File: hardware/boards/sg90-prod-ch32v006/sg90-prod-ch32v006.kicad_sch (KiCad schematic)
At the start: 36 parts, among them J1 Servo Input, J2 Motor, J3 Debug, J4 Potentiometer, Q1 AO3401A, U1 TPAP2210K-3.3TRG1, U2 74LVC2G125, U3 DRV8837DSGR-JSM, U4 CH32V006F8U6

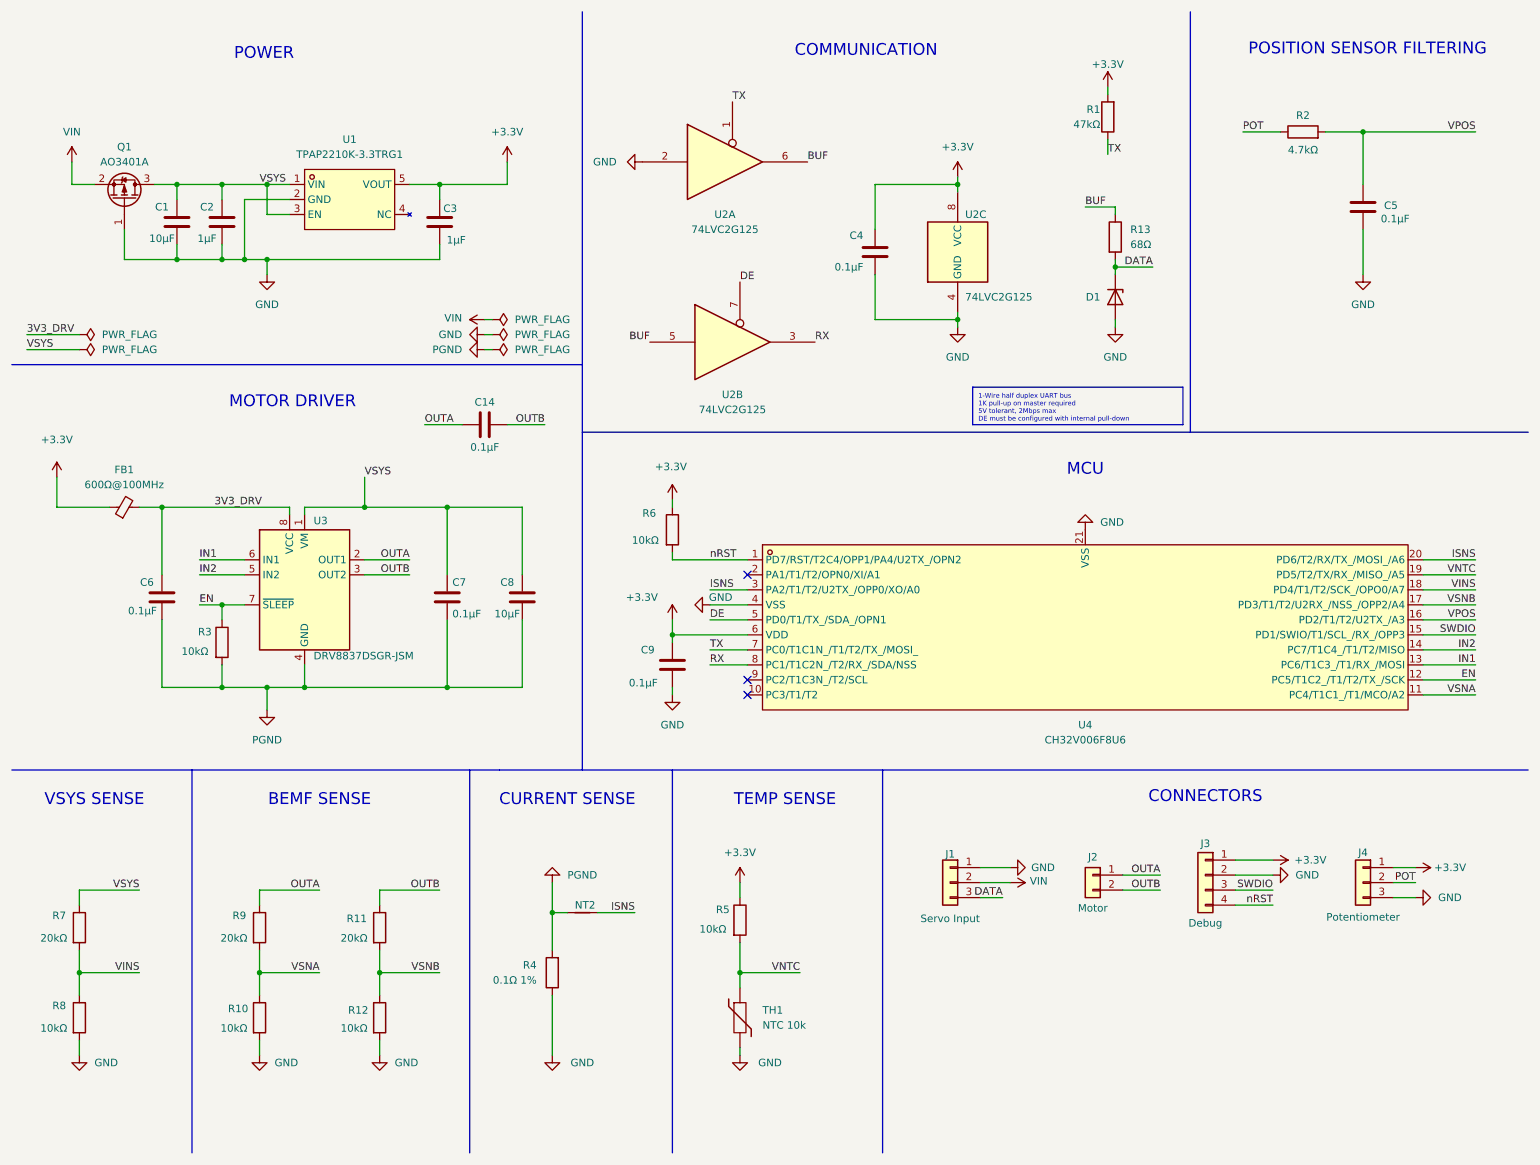
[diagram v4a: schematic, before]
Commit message: update sg90-prod-ch32v006
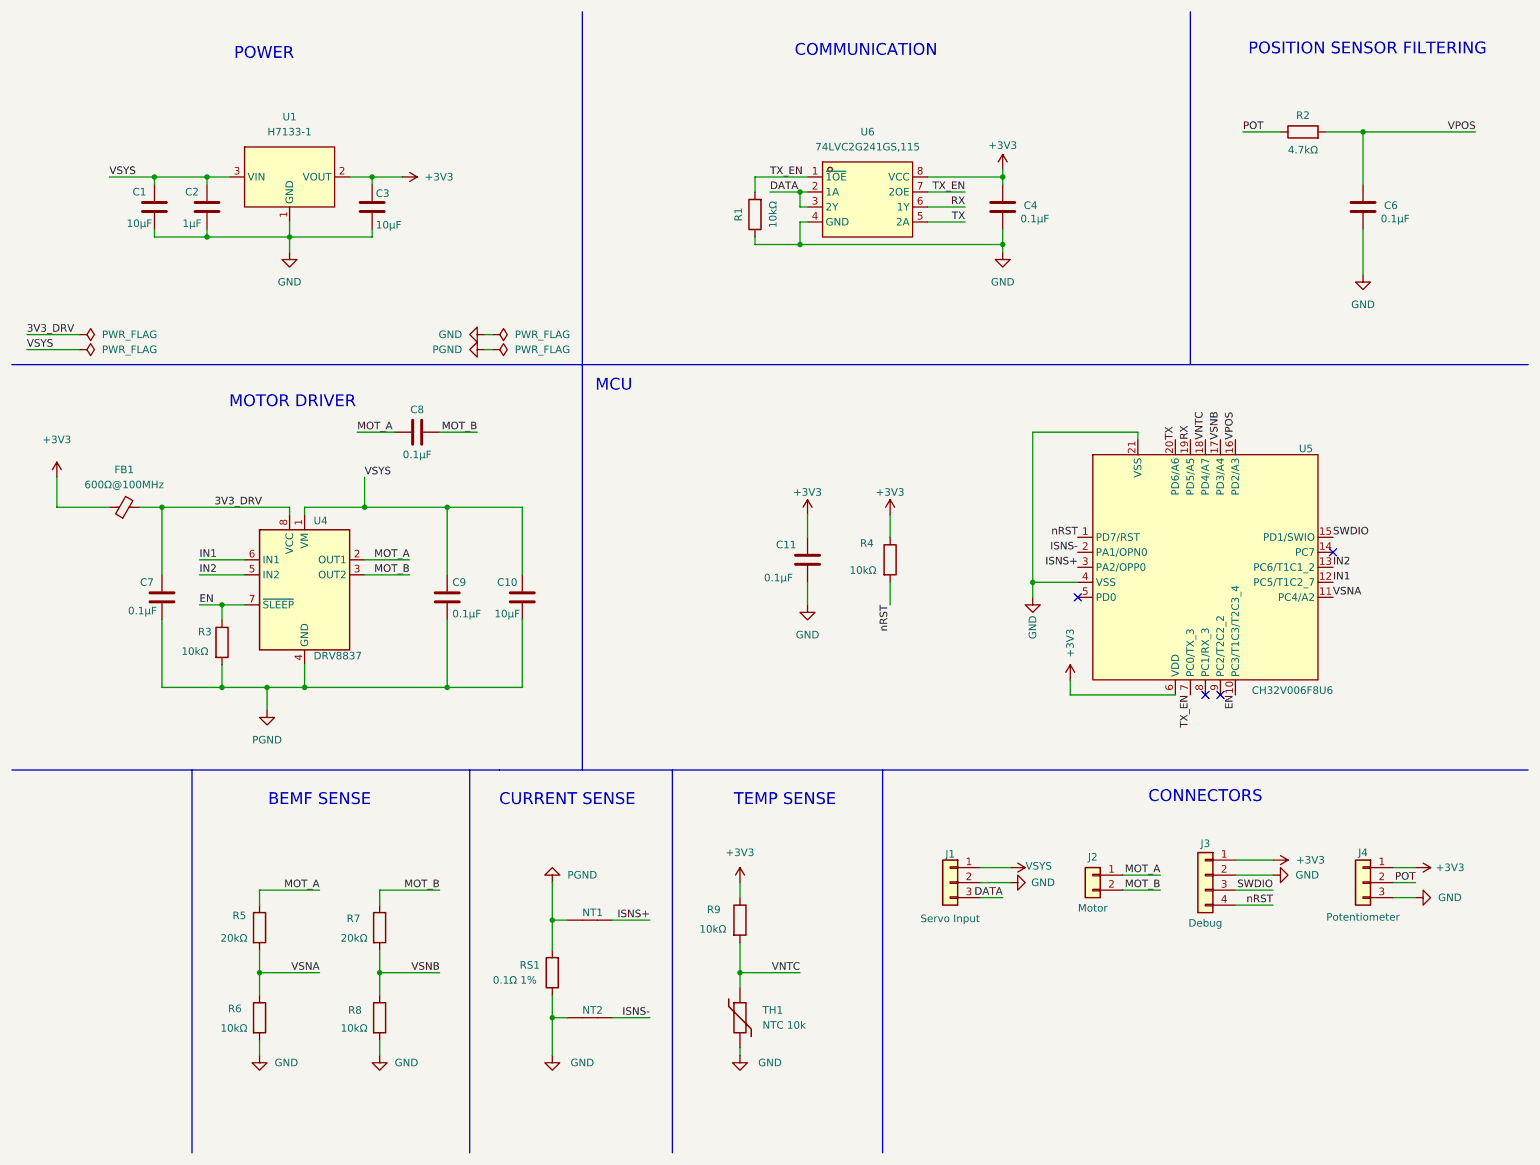
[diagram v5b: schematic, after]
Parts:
- removed D1: ESD, Diode_SMD:D_SOD-882, symbol Diode:PESD5V0L1UL
- removed Q1: AO3401A, Package_TO_SOT_SMD:SOT-23, symbol Transistor_FET:AO3401A
- removed R13: 68Ω, Resistor_SMD:R_0402_1005Metric, symbol Device:R
- removed R7: 20kΩ, Resistor_SMD:R_0402_1005Metric, symbol Device:R
- removed R8: 10kΩ, Resistor_SMD:R_0402_1005Metric, symbol Device:R
- removed U1: TPAP2210K-3.3TRG1, shared:SOT-23-5_L2.9-W1.6-P0.95-LS2.8-BR, symbol shared:TPAP2210K-3.3TRG1
- removed U2: 74LVC2G125, shared:X2-DFN1210-8_L1.2-W1.0-P0.30-BL, symbol 74xGxx:74LVC2G125
- added NT2: NetTie_2, shared:NetTie-2_SMD_0.2mm, symbol Device:NetTie_2
- added U1: H7133-1, shared:SOT-23-3_L2.9-W1.3-P1.90-LS2.4-BR, symbol shared:H7133-1_C277537
- added U6: 74LVC2G241GS,115, shared:XSON-8_L1.4-W1.0-P0.35-S0.55-BL, symbol shared:74LVC2G241GS,115
- C1: JLC Type (none) -> Basic; MFPN (none) -> CL10A106MA8NRNC
- C10: renamed from C8; JLC Type (none) -> Basic; MFPN (none) -> CL10A106MA8NRNC
- C11: renamed from C9; JLC Type (none) -> Basic; MFPN (none) -> CL05B104KO5NNNC
- C2: JLC Type (none) -> Basic; MFPN (none) -> CL05A105KA5NQNC
- C3: value 1µF -> 10µF; JLC Type (none) -> Basic; LCSC C52923 -> C15525; MFPN (none) -> CL05A106MQ5NUNC
- C4: JLC Type (none) -> Basic; MFPN (none) -> CL05B104KO5NNNC
- C6: renamed from C5; JLC Type (none) -> Basic; MFPN (none) -> CL05B104KO5NNNC
- C7: renamed from C6; JLC Type (none) -> Basic; MFPN (none) -> CL05B104KO5NNNC
- C8: renamed from C14; JLC Type (none) -> Basic; MFPN (none) -> CL05B104KO5NNNC
- C9: renamed from C7; JLC Type (none) -> Basic; MFPN (none) -> CL05B104KO5NNNC
- FB1: footprint Inductor_SMD:L_0603_1608Metric -> Inductor_SMD:L_0402_1005Metric; JLC Type (none) -> Extended; LCSC C1002 -> C76884; MFPN (none) -> BLM15AG601SN1D
- R1: value 47kΩ -> 10kΩ; JLC Type (none) -> Basic; LCSC C25792 -> C25744; MFPN (none) -> 0402WGF1002TCE
- R2: JLC Type (none) -> Basic; MFPN (none) -> 0402WGF4701TCE
- R3: JLC Type (none) -> Basic; MFPN (none) -> 0402WGF1002TCE
- R4: renamed from R6; JLC Type (none) -> Basic; MFPN (none) -> 0402WGF1002TCE
- R5: renamed from R9; JLC Type (none) -> Basic; MFPN (none) -> 0402WGF2003TCE
- R6: renamed from R10; JLC Type (none) -> Basic; MFPN (none) -> 0402WGF1002TCE
- R7: renamed from R11; JLC Type (none) -> Basic; MFPN (none) -> 0402WGF2003TCE
- R8: renamed from R12; JLC Type (none) -> Basic; MFPN (none) -> 0402WGF1002TCE
- R9: renamed from R5; JLC Type (none) -> Basic; MFPN (none) -> 0402WGF1002TCE
- RS1: renamed from R4; JLC Type (none) -> Basic; MFPN (none) -> 1206W4F100LT5E
- TH1: JLC Type (none) -> Extended; MFPN (none) -> NCP15XH103F03RC
- U4: renamed from U3; value DRV8837DSGR-JSM -> DRV8837; JLC Type (none) -> Extended; LCSC C22447132 -> C39159; MFPN (none) -> DRV8837DSGR
- U5: renamed from U4; JLC Type (none) -> Extended; LCSC Part C42431288 -> (none); MFPN (none) -> CH32V006F8U6
- renumbered NT2 to NT1
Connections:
- net VIN is gone; now on net GND: J1.2 (Pin_2)
- net VINS is gone; now on net VNTC: U5.18 (PD4/A7)
- net DATA: now also U6.2 (1A), U6.3 (2Y)
- net EN: now also U5.10 (PC3/T1C3/T2C3_4); no longer U5.12 (PC5/T1C2_/T1/T2/TX_/SCK)
- net GND: now also R1.1, NT2.2, U1.1 (GND), U6.4 (GND); no longer J1.1 (Pin_1)
- net IN1: now also U5.12 (PC5/T1C2_7); no longer U5.13 (PC6/T1C3_/T1/RX_/MOSI)
- net IN2: now also U5.13 (PC6/T1C1_2); no longer U5.14 (PC7/T1C4_/T1/T2/MISO)
- net RX: now also U5.19 (PD5/A5), U6.6 (1Y); no longer U5.8 (PC1/T1C2N_/T2/RX_/SDA/NSS)
- net TX: now also U5.20 (PD6/A6), U6.5 (2A); no longer R1.1, U5.7 (PC0/T1C1N_/T1/T2/TX_/MOSI_)
- net VNTC: no longer U5.19 (PD5/T2/TX/RX_/MISO_/A5)
- net VSYS: now also J1.1 (Pin_1), U1.3 (VIN)
- net ISNS-: now reaches U5.2 (PA1/OPN0)
- net ISNS-: now also NT2.1
- net +3.3V renamed +3V3
- net +3V3: now also U1.2 (VOUT), U6.8 (VCC); no longer R1.2
- net DE: no longer names the net of U5.5 (PD0)
- net ISNS renamed ISNS+
- net ISNS+: no longer U5.20 (PD6/T2/RX/TX_/MOSI_/A6)
- net OUTA renamed MOT_A
- net OUTB renamed MOT_B
- new net TX_EN: R1.2, U5.7 (PC0/TX_3), U6.1 (~{1OE}), U6.7 (2OE)
- no-connect marks 3 -> 4
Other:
- note removed: "VSYS SENSE"
- moved on the sheet: C1, C11, C3, C8, NT1, R4

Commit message: rebuilt board
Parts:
- removed C1: 10µF, Capacitor_SMD:C_0603_1608Metric, symbol Device:C
- removed U1: H7133-1, shared:SOT-23-3_L2.9-W1.3-P1.90-LS2.4-BR, symbol shared:H7133-1_C277537
- added U1: TLV76733DRVR, Package_SON:WSON-6-1EP_2x2mm_P0.65mm_EP1x1.6mm, symbol Regulator_Linear:TLV76733DRVx
- C2: renamed from C3; value 10µF -> 4.7µF; LCSC C15525 -> C23733; MFPN CL05A106MQ5NUNC -> CL05A475MP5NRNC
- NT1, NT2: footprint shared:NetTie-2_SMD_0.2mm -> shared:NetTie-2_SMD_0.127mm
- RS1: value 0.1Ω 1% -> 10mΩ 1%; footprint Resistor_SMD:R_1206_3216Metric -> Resistor_SMD:R_0805_2012Metric; JLC Type Basic -> Extended; LCSC C25334 -> C163089; MFPN 1206W4F100LT5E -> RLM10FTSMR010
- renumbered C2 to C1
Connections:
- net +3V3: now also U1.1 (OUT), U1.2 (SNS)
- net EN: now also U5.14 (PC7); no longer U5.10 (PC3/T1C3/T2C3_4)
- net GND: now also U1.3 (GND), U1.5 (GND), U1.7 (PAD)
- net IN1: now also U5.13 (PC6/T1C1_2); no longer U5.12 (PC5/T1C2_7)
- net IN2: now also U5.12 (PC5/T1C2_7); no longer U5.13 (PC6/T1C1_2)
- net RX: now also U5.8 (PC1/RX_3); no longer U5.19 (PD5/A5)
- net TX: now also U5.7 (PC0/TX_3); no longer U5.20 (PD6/A6)
- net TX_EN: now also U5.9 (PC2/T2C2_2); no longer U5.7 (PC0/TX_3)
- net VSNA: now also U5.17 (PD3/A4); no longer U5.11 (PC4/A2)
- net VSNB: now also U5.11 (PC4/A2); no longer U5.17 (PD3/A4)
- net VSYS: now also U1.4 (EN), U1.6 (IN)
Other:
- moved on the sheet: C1, C2, NT1, NT2

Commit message: wip
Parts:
- removed U1: TLV76733DRVR, Package_SON:WSON-6-1EP_2x2mm_P0.65mm_EP1x1.6mm, symbol Regulator_Linear:TLV76733DRVx
- added U1: H7133-1_C277537, shared:SOT-23-3_L2.9-W1.3-P1.90-LS2.4-BR, symbol shared:H7133-1_C277537
- C1: value 1µF -> 10µF; footprint Capacitor_SMD:C_0402_1005Metric -> Capacitor_SMD:C_0603_1608Metric; LCSC C52923 -> C96446; MFPN CL05A105KA5NQNC -> CL10A106MA8NRNC
- C2: value 4.7µF -> 10µF; footprint Capacitor_SMD:C_0402_1005Metric -> Capacitor_SMD:C_0603_1608Metric; LCSC C23733 -> C96446; MFPN CL05A475MP5NRNC -> CL10A106MA8NRNC
- R5, R7: LCSC C25764 -> C25765; MFPN 0402WGF2003TCE -> 0402WGF2002TCE
- U6: JLC Type (none) -> Extended; MFPN (none) -> 74LVC2G241GS,115
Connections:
- net +3V3: now also J4.3 (Pin_3), U1.2 (VOUT); no longer J4.1 (Pin_1)
- net EN: now also U5.12 (PC5/T1C2_7); no longer U5.14 (PC7)
- net GND: now also J1.1 (Pin_1), J4.1 (Pin_1), U1.1 (GND); no longer J1.2 (Pin_2), J4.3 (Pin_3)
- net IN2: now also U5.14 (PC7/T1C3_3); no longer U5.12 (PC5/T1C2_7)
- net TX_EN: now also U5.5 (PD0/TX_2); no longer U5.9 (PC2/T2C2_2)
- net VSNA: now also U5.11 (PC4/A2); no longer U5.17 (PD3/A4)
- net VSNB: now also U5.17 (PD3/A4); no longer U5.11 (PC4/A2)
- net VSYS: now also J1.2 (Pin_2), U1.3 (VIN); no longer J1.1 (Pin_1)
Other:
- moved on the sheet: C1, C2, U5
